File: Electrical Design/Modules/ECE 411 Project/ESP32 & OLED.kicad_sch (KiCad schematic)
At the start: 1 part, among them U11 ESP32-WROOM-32

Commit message: PCB V2!!!
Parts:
- removed U11: ESP32-WROOM-32, RF_Module:ESP32-WROOM-32, symbol RF_Module:ESP32-WROOM-32
- added U6: ~, Module:PinHeader_ESP32_WROOM_Narrow, symbol RF_Module:ESP32-WROOM-D2-NHeader
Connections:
- net +5V: now also U6.19 (5V)
- net BTN0: now also U6.35 (TXD0/IO1)
- net BTN1: now also U6.33 (IO21)
- net BTN2: now also U6.31 (IO19)
- net BTN3: now also U6.30 (IO18)
- net BTN4: now also U6.29 (IO5)
- net BTN5: now also U6.28 (IO17)
- net BTN6: now also U6.27 (IO16)
- net BTN7: now also U6.23 (IO15)
- net CLK: now also U6.24 (IO2)
- net GENOUT: now also U6.9 (IO33)
- net GND: now also U6.14 (GND), U6.15 (IO13), U6.2 (EN), U6.38 (GND), U6.39 (GND)
- net SCL: now also U6.13 (IO12)
- net SDA: now also U6.15 (IO13)

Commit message: schematic changes
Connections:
- net BTN0: now also U6.31 (IO19); no longer U6.35 (TXD0/IO1)
- net BTN1: now also U6.30 (IO18); no longer U6.33 (IO21)
- net BTN2: now also U6.29 (IO5); no longer U6.31 (IO19)
- net BTN3: now also U6.28 (IO17); no longer U6.30 (IO18)
- net BTN4: now also U6.27 (IO16); no longer U6.29 (IO5)
- net BTN5: now also U6.26 (IO4); no longer U6.28 (IO17)
- net BTN6: now also U6.25 (IO0); no longer U6.27 (IO16)
- net SCL: now also U6.36 (IO22); no longer U6.13 (IO12)
- net SDA: now also U6.33 (IO21); no longer U6.15 (IO13)
- net BTN7: no longer names the net of U6.23 (IO15)
- net CLK: no longer names the net of U6.24 (IO2)
- no-connect marks 21 -> 24
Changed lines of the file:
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@@
 	)
 	(no_connect
-		(at 159.385 64.135)
+		(at 159.385 97.155)
 	)
 	(no_connect
@@
 	)
 	(no_connect
+		(at 159.385 92.075)
+	)
+	(no_connect
 		(at 159.385 120.015)
 	)
@@
 	)
 	(no_connect
-		(at 159.385 86.995)
+		(at 159.385 94.615)
+	)
+	(no_connect
+		(at 159.385 66.675)
 	)
 	(no_connect
@@
 	)
 	(no_connect
+		(at 159.385 122.555)
+	)
+	(no_connect
 		(at 128.905 66.675)
 	)
@@
 	)
 	(no_connect
-		(at 159.385 89.535)
-	)
-	(no_connect
 		(at 159.385 69.215)
 	)
@@
 		(at 159.385 107.315)
 	)
+	(no_connect
+		(at 159.385 99.695)
+	)
 	(wire
 		(pts
@@
 	(wire
 		(pts
+			(xy 159.385 84.455) (xy 165.735 84.455)
+		)
+		(stroke
+			(width 0)
+			(type default)
+		)
+	)
+	(wire
+		(pts
+			(xy 159.385 109.855) (xy 165.735 109.855)
+		)
+		(stroke
+			(width 0)
+			(type default)
+		)
+	)
+	(wire
+		(pts
+			(xy 159.385 86.995) (xy 165.735 86.995)
+		)
+		(stroke
+			(width 0)
+			(type default)
+		)
+	)
+	(wire
+		(pts
 			(xy 159.385 79.375) (xy 165.735 79.375)
 		)
@@
 	(wire
 		(pts
-			(xy 159.385 94.615) (xy 165.735 94.615)
-		)
-		(stroke
-			(width 0)
-			(type default)
-		)
-	)
-	(wire
-		(pts
-			(xy 159.385 109.855) (xy 165.735 109.855)
+			(xy 159.385 76.835) (xy 165.735 76.835)
+		)
+		(stroke
+			(width 0)
+			(type default)
+		)
+	)
+	(wire
+		(pts
+			(xy 159.385 71.755) (xy 165.735 71.755)
 		)
 		(stroke
@@
 	(wire
 		(pts
-			(xy 159.385 71.755) (xy 165.735 71.755)
-		)
-		(stroke
-			(width 0)
-			(type default)
-		)
-	)
-	(wire
-		(pts
-			(xy 159.385 97.155) (xy 165.735 97.155)
-		)
-		(stroke
-			(width 0)
-			(type default)
-		)
-	)
-	(wire
-		(pts
-			(xy 159.385 76.835) (xy 165.735 76.835)
-		)
-		(stroke
-			(width 0)
-			(type default)
-		)
-	)
-	(wire
-		(pts
-			(xy 159.385 92.075) (xy 165.735 92.075)
-		)
-		(stroke
-			(width 0)
-			(type default)
-		)
-	)
-	(wire
-		(pts
-			(xy 159.385 66.675) (xy 165.735 66.675)
-		)
-		(stroke
-			(width 0)
-			(type default)
-		)
-	)
-	(wire
-		(pts
 			(xy 144.145 127.635) (xy 144.145 140.335)
 		)
@@
 	(wire
 		(pts
-			(xy 159.385 99.695) (xy 165.735 99.695)
-		)
-		(stroke
-			(width 0)
-			(type default)
-		)
-	)
-	(wire
-		(pts
-			(xy 159.385 84.455) (xy 165.735 84.455)
+			(xy 159.385 64.135) (xy 165.735 64.135)
+		)
+		(stroke
+			(width 0)
+			(type default)
+		)
+	)
+	(wire
+		(pts
+			(xy 159.385 89.535) (xy 165.735 89.535)
 		)
 		(stroke
@@
 	(hierarchical_label "BTN2"
 		(shape input)
+		(at 165.735 79.375 0)
+		(fields_autoplaced yes)
+		(effects
+			(font
+				(size 1.27 1.27)
+			)
+			(justify left)
+		)
+	)
+	(hierarchical_label "BTN0"
+		(shape input)
 		(at 165.735 74.295 0)
 		(fields_autoplaced yes)
@@
 		)
 	)
-	(hierarchical_label "CLK"
-		(shape output)
-		(at 165.735 92.075 0)
+	(hierarchical_label "BTN3"
+		(shape input)
+		(at 165.735 81.915 0)
 		(fields_autoplaced yes)
 		(effects
@@
 		)
 	)
-	(hierarchical_label "BTN0"
+	(hierarchical_label "BTN4"
 		(shape input)
-		(at 165.735 66.675 0)
+		(at 165.735 84.455 0)
 		(fields_autoplaced yes)
 		(effects
@@
 		)
 	)
-	(hierarchical_label "BTN3"
+	(hierarchical_label "BTN5"
+		(shape input)
+		(at 165.735 86.995 0)
+		(fields_autoplaced yes)
+		(effects
+			(font
+				(size 1.27 1.27)
+			)
+			(justify left)
+		)
+	)
+	(hierarchical_label "SCL"
+		(shape bidirectional)
+		(at 165.735 64.135 0)
+		(fields_autoplaced yes)
+		(effects
+			(font
+				(size 1.27 1.27)
+			)
+			(justify left)
+		)
+	)
+	(hierarchical_label "BTN1"
 		(shape input)
 		(at 165.735 76.835 0)
@@
 		)
 	)
-	(hierarchical_label "BTN4"
+	(hierarchical_label "BTN6"
 		(shape input)
-		(at 165.735 79.375 0)
+		(at 165.735 89.535 0)
 		(fields_autoplaced yes)
 		(effects
@@
 		)
 	)
-	(hierarchical_label "BTN5"
-		(shape input)
-		(at 165.735 81.915 0)
-		(fields_autoplaced yes)
-		(effects
-			(font
-				(size 1.27 1.27)
-			)
-			(justify left)
-		)
-	)
-	(hierarchical_label "SCL"
+	(hierarchical_label "SDA"
 		(shape bidirectional)
-		(at 165.735 99.695 0)
-		(fields_autoplaced yes)
-		(effects
-			(font
-				(size 1.27 1.27)
-			)
-			(justify left)
-		)
-	)
-	(hierarchical_label "BTN7"
-		(shape input)
-		(at 165.735 94.615 0)
-		(fields_autoplaced yes)
-		(effects
-			(font
-				(size 1.27 1.27)
-			)
-			(justify left)
-		)
-	)
-	(hierarchical_label "BTN1"
-		(shape input)
 		(at 165.735 71.755 0)
 		(fields_autoplaced yes)
 		(effects
-			(font
-				(size 1.27 1.27)
-			)
-			(justify left)
-		)
-	)
-	(hierarchical_label "BTN6"
-		(shape input)
-		(at 165.735 84.455 0)
-		(fields_autoplaced yes)
-		(effects
-			(font
-				(size 1.27 1.27)
-			)
-			(justify left)
-		)
-	)
-	(hierarchical_label "SDA"
-		(shape bidirectional)
-		(at 165.735 97.155 0)
-		(fields_autoplaced yes)
-		(effects

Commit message: pcb redo b2.1
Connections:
- net BTN0: now also U6.13 (IO12); no longer U6.31 (IO19)
- net BTN1: now also U6.12 (IO14); no longer U6.30 (IO18)
- net BTN2: now also U6.11 (IO27); no longer U6.29 (IO5)
- net BTN3: now also U6.10 (IO26); no longer U6.28 (IO17)
- net BTN4: now also U6.9 (IO25); no longer U6.27 (IO16)
- net BTN5: now also U6.8 (IO33); no longer U6.26 (IO4)
- net BTN6: now also U6.7 (IO32); no longer U6.25 (IO0)
- net GENOUT: now also U6.6 (IO35); no longer U6.9 (IO33)
- net MCU3v3: now reaches U6.1 (3V3)
- net FREQ: now reaches U6.5 (IO34)
- no-connect marks 24 -> 14
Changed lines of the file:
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@@
-	)
-	(no_connect
-		(at 159.385 104.775)
 	)
 	(no_connect
@@
 	)
 	(no_connect
-		(at 144.145 56.515)
+		(at 128.905 97.155)
+	)
+	(no_connect
+		(at 159.385 92.075)
+	)
+	(no_connect
+		(at 128.905 92.075)
+	)
+	(no_connect
+		(at 159.385 94.615)
+	)
+	(no_connect
+		(at 159.385 66.675)
+	)
+	(no_connect
+		(at 128.905 66.675)
+	)
+	(no_connect
+		(at 128.905 104.775)
 	)
 	(no_connect
@@
 	)
 	(no_connect
-		(at 128.905 97.155)
-	)
-	(no_connect
-		(at 159.385 92.075)
-	)
-	(no_connect
-		(at 159.385 120.015)
-	)
-	(no_connect
-		(at 159.385 117.475)
-	)
-	(no_connect
-		(at 128.905 92.075)
-	)
-	(no_connect
-		(at 159.385 102.235)
-	)
-	(no_connect
-		(at 159.385 94.615)
-	)
-	(no_connect
-		(at 159.385 66.675)
-	)
-	(no_connect
-		(at 159.385 112.395)
-	)
-	(no_connect
-		(at 159.385 114.935)
-	)
-	(no_connect
-		(at 159.385 122.555)
-	)
-	(no_connect
-		(at 128.905 66.675)
-	)
-	(no_connect
-		(at 128.905 104.775)
-	)
-	(no_connect
 		(at 159.385 69.215)
 	)
@@
 		(at 128.905 69.215)
 	)
-	(no_connect
-		(at 159.385 107.315)
-	)
-	(no_connect
-		(at 159.385 99.695)
-	)
 	(wire
 		(pts
@@
 	(wire
 		(pts
-			(xy 159.385 84.455) (xy 165.735 84.455)
-		)
-		(stroke
-			(width 0)
-			(type default)
-		)
-	)
-	(wire
-		(pts
 			(xy 159.385 109.855) (xy 165.735 109.855)
 		)
@@
 	(wire
 		(pts
-			(xy 159.385 86.995) (xy 165.735 86.995)
-		)
-		(stroke
-			(width 0)
-			(type default)
-		)
-	)
-	(wire
-		(pts
-			(xy 159.385 79.375) (xy 165.735 79.375)
-		)
-		(stroke
-			(width 0)
-			(type default)
-		)
-	)
-	(wire
-		(pts
-			(xy 159.385 76.835) (xy 165.735 76.835)
+			(xy 159.385 117.475) (xy 165.735 117.475)
+		)
+		(stroke
+			(width 0)
+			(type default)
+		)
+	)
+	(wire
+		(pts
+			(xy 159.385 102.235) (xy 165.735 102.235)
+		)
+		(stroke
+			(width 0)
+			(type default)
+		)
+	)
+	(wire
+		(pts
+			(xy 144.145 48.26) (xy 144.145 56.515)
 		)
 		(stroke
@@
 	(wire
 		(pts
-			(xy 159.385 81.915) (xy 165.735 81.915)
-		)
-		(stroke
-			(width 0)
-			(type default)
-		)
-	)
-	(wire
-		(pts
-			(xy 159.385 74.295) (xy 165.735 74.295)
+			(xy 159.385 99.695) (xy 165.735 99.695)
+		)
+		(stroke
+			(width 0)
+			(type default)
+		)
+	)
+	(wire
+		(pts
+			(xy 159.385 120.015) (xy 165.735 120.015)
+		)
+		(stroke
+			(width 0)
+			(type default)
+		)
+	)
+	(wire
+		(pts
+			(xy 159.385 104.775) (xy 165.735 104.775)
 		)
 		(stroke
@@
 	(wire
 		(pts
+			(xy 159.385 107.315) (xy 165.735 107.315)
+		)
+		(stroke
+			(width 0)
+			(type default)
+		)
+	)
+	(wire
+		(pts
 			(xy 147.955 48.26) (xy 147.955 56.515)
 		)
@@
 	(wire
 		(pts
-			(xy 159.385 89.535) (xy 165.735 89.535)
+			(xy 159.385 114.935) (xy 165.735 114.935)
+		)
+		(stroke
+			(width 0)
+			(type default)
+		)
+	)
+	(wire
+		(pts
+			(xy 159.385 112.395) (xy 165.735 112.395)
 		)
 		(stroke
@@
 		)
 	)
-	(hierarchical_label "BTN2"
+	(hierarchical_label "GENOUT"
 		(shape input)
-		(at 165.735 79.375 0)
+		(at 165.735 117.475 0)
 		(fields_autoplaced yes)
 		(effects
@@
 		)
 	)
-	(hierarchical_label "BTN0"
+	(hierarchical_label "MCU3v3"
 		(shape input)
-		(at 165.735 74.295 0)
+		(at 144.145 48.26 90)
 		(fields_autoplaced yes)
 		(effects
@@
 		)
 	)
-	(hierarchical_label "BTN3"
+	(hierarchical_label "BTN0"
 		(shape input)
-		(at 165.735 81.915 0)
+		(at 165.735 99.695 0)
 		(fields_autoplaced yes)
 		(effects
@@
 	(hierarchical_label "BTN4"
 		(shape input)
-		(at 165.735 84.455 0)
+		(at 165.735 109.855 0)
 		(fields_autoplaced yes)
 		(effects
@@
 	(hierarchical_label "BTN5"
 		(shape input)
-		(at 165.735 86.995 0)
+		(at 165.735 112.395 0)
 		(fields_autoplaced yes)
 		(effects
@@
 	(hierarchical_label "BTN1"
 		(shape input)
-		(at 165.735 76.835 0)
+		(at 165.735 102.235 0)
 		(fields_autoplaced yes)
 		(effects
@@
 		)
 	)
-	(hierarchical_label "BTN6"
+	(hierarchical_label "BTN3"
 		(shape input)
-		(at 165.735 89.535 0)
+		(at 165.735 107.315 0)
 		(fields_autoplaced yes)
 		(effects
@@
 		)
 	)
+	(hierarchical_label "FREQ"
+		(shape input)
+		(at 165.735 120.015 0)
+		(fields_autoplaced yes)
+		(effects
+			(font
+				(size 1.27 1.27)
+			)
+			(justify left)
+		)
+	)
+	(hierarchical_label "BTN6"
+		(shape input)
+		(at 165.735 114.935 0)
+		(fields_autoplaced yes)
+		(effects
+			(font
+				(size 1.27 1.27)
+			)
+			(justify left)
+		)
+	)
+	(hierarchical_label "BTN2"
+		(shape input)
+		(at 165.735 104.775 0)
+		(fields_autoplaced yes)
+		(effects
+			(font
+				(size 1.27 1.27)
+			)
+			(justify left)
+		)
+	)
 	(hierarchical_label "SDA"
 		(shape bidirectional)
 		(at 165.735 71.755 0)
-		(fields_autoplaced yes)
-		(effects
-			(font
-				(size 1.27 1.27)
-			)
-			(justify left)
-		)
-	)
-	(hierarchical_label "GENOUT"
-		(shape output)
-		(at 165.735 109.855 0)
 		(fields_autoplaced yes)
 		(effects
@@
 		)
 		(pin "9"
-		)
-		(pin "9"

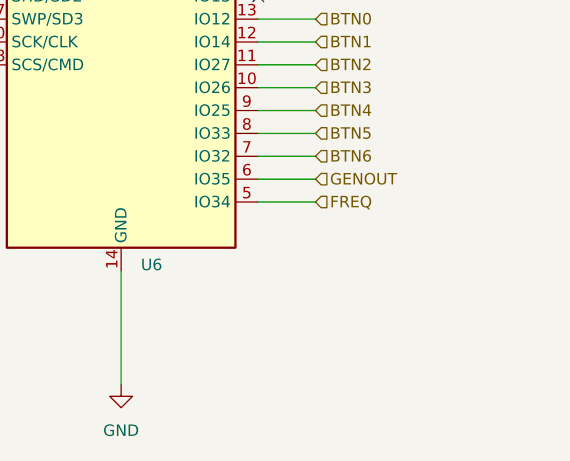
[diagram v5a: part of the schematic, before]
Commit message: new space-optimized PCB layout
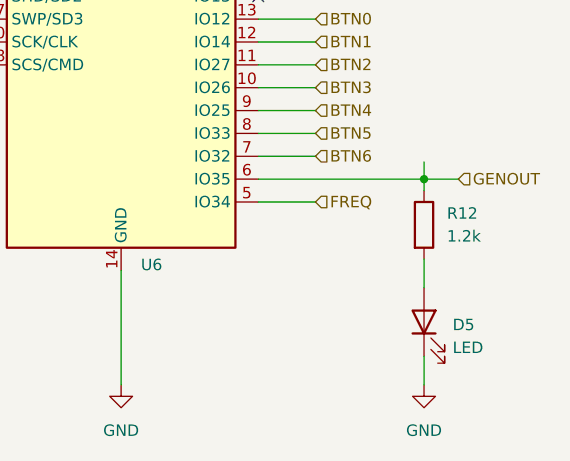
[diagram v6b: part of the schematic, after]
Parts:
- added D5: LED, LED_THT:LED_D5.0mm, symbol Device:LED
- added R12: 1.2k, Resistor_SMD:R_0805_2012Metric_Pad1.20x1.40mm_HandSolder, symbol Device:R
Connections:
- net GENOUT: now also R12.1
- net GND: now also D5.1 (K)
- new net: D5.2 (A), R12.2

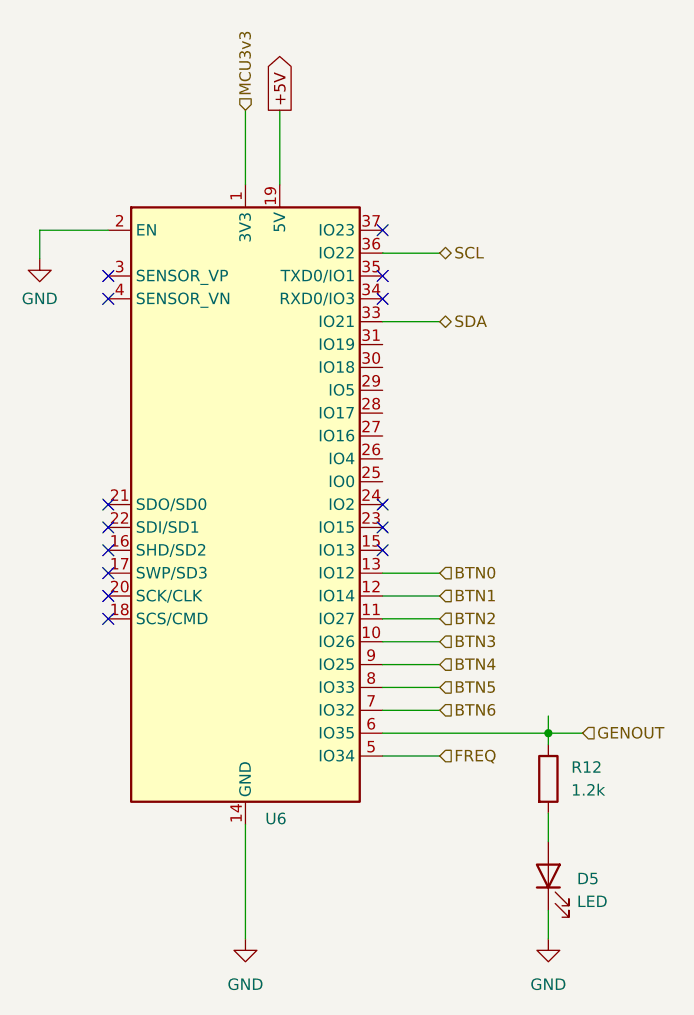
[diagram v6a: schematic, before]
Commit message: update diode footptint, rounding edge cuts, some stitching
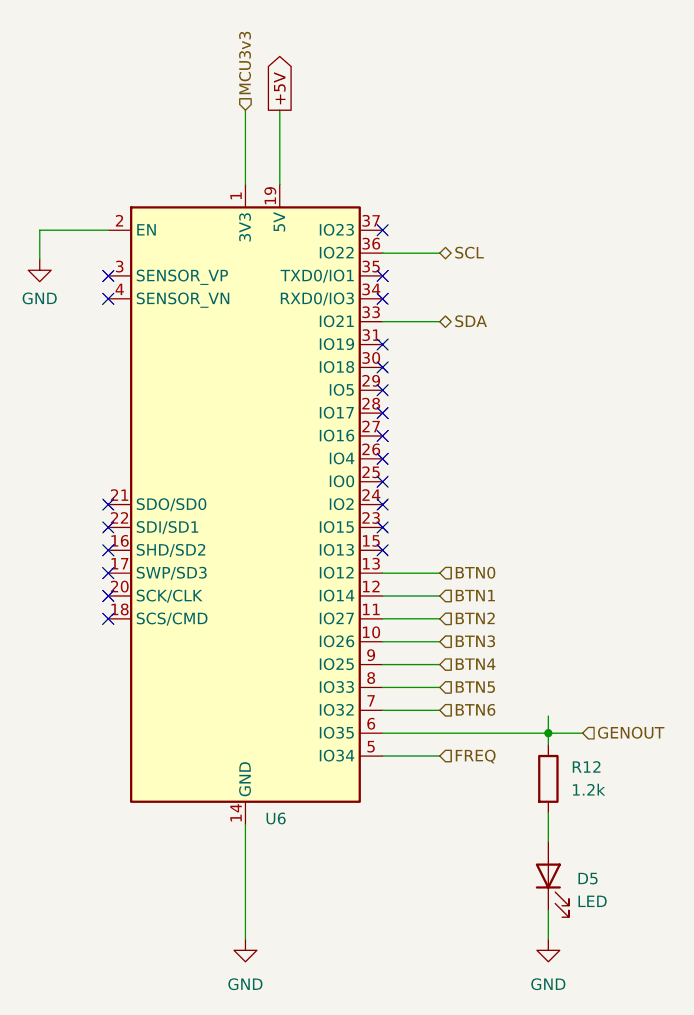
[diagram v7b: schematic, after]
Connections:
- no-connect marks 14 -> 21
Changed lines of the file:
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@@
 	(title_block
 		(title "ESP32 Microcontroller Module")
-		(date "2024-11-14")
-		(rev "1.7")
+		(date "2024-11-18")
+		(rev "1.8")
 		(company "Portland State University")
 		(comment 1 "Open Source Hardware")
@@
 	)
 	(no_connect
+		(at 159.385 84.455)
+	)
+	(no_connect
 		(at 159.385 61.595)
 	)
 	(no_connect
+		(at 159.385 74.295)
+	)
+	(no_connect
 		(at 128.905 99.695)
+	)
+	(no_connect
+		(at 159.385 79.375)
+	)
+	(no_connect
+		(at 159.385 76.835)
 	)
 	(no_connect
@@
 	)
 	(no_connect
+		(at 159.385 81.915)
+	)
+	(no_connect
+		(at 159.385 86.995)
+	)
+	(no_connect
+		(at 159.385 89.535)
+	)
+	(no_connect

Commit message: pcb madness
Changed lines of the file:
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@@
-	(wire
-		(pts
-			(xy 177.8 115.57) (xy 177.8 117.475)
-		)
-		(stroke
-			(width 0)
-			(type default)
-		)
-	)
 	(wire
 		(pts
